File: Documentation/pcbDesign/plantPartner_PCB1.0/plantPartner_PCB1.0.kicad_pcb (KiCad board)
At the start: 2 copper layers, 271 x 152 mm, 76 parts, among them IC1 MPM3610, J1 Conn_01x04, J10 Screw_Terminal_01x03, J11 Conn_01x04, J12 Conn_01x03, J13 Conn_01x03, J14 Conn_01x03, J15 Conn_01x03, J16 Conn_01x04, J17 Conn_01x03, J18 Screw_Terminal_01x02, J19 Barrel_Jack, J2 Conn_01x04, J20 Conn_02x04_Top_Bottom, J21 Conn_01x04, J22 Conn_01x04, J23 Conn_01x02, J24 Conn_01x04, J25 Conn_01x04, J26 Conn_01x01, J27 Conn_01x03, J3 Conn_01x04, J4 Screw_Terminal, J5 Conn_01x02, J6 Screw_Terminal_01x03, J7 Conn_01x03, J8 Conn_02x04_Top_Bottom, J9 Conn_01x03, K1 SRD-05VDC-SL-C, K2 SRD-05VDC-SL-C, Q1 PNP, Q2 PNP, U1 EL357N-G, U2 MAX485, U3 ESP32-DEVKIT-V1, U4 EL357N-G

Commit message: Finished RS485 Transceiver, working on Buck Converter and connecting signals
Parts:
- removed J24: Conn_01x04, Connector_PinHeader_2.54mm:PinHeader_1x04_P2.54mm_Vertical
- J11: value Conn_01x04 -> Conn_01x02; footprint Connector_PinHeader_2.54mm:PinHeader_1x04_P2.54mm_Vertical -> Connector_PinHeader_2.54mm:PinHeader_1x02_P2.54mm_Vertical
- moved J26 118.7 mm to (222.2, 54.5)
- moved J11 61.8 mm to (81.7, 46.6), turned to 180 degrees
- moved R24 54.3 mm to (245.5, 25.1), turned to 0 degrees
- moved J17 50.4 mm to (242.7, 37.8)
- moved J5 49.3 mm to (243.0, 25.0)
- moved J20 45.3 mm to (177.3, 59.1), turned to 180 degrees
- moved D5 45.1 mm to (229.3, 60.5)
- moved D7 45.1 mm to (234.6, 57.7)
- moved J13 45.1 mm to (252.3, 72.6)
- moved K2 45.1 mm to (246.1, 62.7)
- moved Q2 45.1 mm to (234.3, 61.5)
- moved R18 45.1 mm to (229.0, 65.7)
- moved R20 45.1 mm to (235.3, 65.0)
- moved U4 45.1 mm to (231.8, 68.5)
- moved D6 45.1 mm to (234.7, 55.3)
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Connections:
- J11 pad 1: /B -> GND
- J11 pad 2: /A -> +12V
- J20 pad 3: /ADC1_5/Touch8 -> /ADC1_4/Touch9
- J20 pad 4: /ADC2_0/Touch0 -> /ADC1_5/Touch8
- J20 pad 8: /ADC1_4/Touch9 -> /ADC2_0/Touch0
- J26 pad 1: +12V -> /PWM_WATER_PIN
- J27 pad 1: +12V -> /PWM_FERTIL_PIN
- U1 pad 2: +12V -> /PWM_FERTIL_PIN
- U3 pad 27: +12V -> /PWM_WATER_PIN
- U3 pad 28: +12V -> /PWM_FERTIL_PIN
- U4 pad 2: +12V -> /PWM_WATER_PIN
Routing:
- net +12V: track 44.1 -> 101.1 mm, vias 0 -> 2
- net /ADC2_0/Touch0: track 0.00 -> 51.8 mm
- net /PWM_WATER_PIN: track 0.00 -> 19.5 mm
- net /B: track 2.79 -> 19.2 mm
- net /ADC1_6: track 0.00 -> 15.4 mm
- net /A: track 2.76 -> 17.6 mm
- net /ADC2_8/DAC1: track 0.00 -> 14.7 mm
- net /ADC2_7/Touch7: track 0.00 -> 14.6 mm
- net /ADC1_4/Touch9: track 0.00 -> 14.3 mm
- net GND: track 95.1 -> 107.2 mm
- net /ADC2_9/DAC2: track 0.00 -> 12.0 mm
- net /ADC1_7: track 0.00 -> 11.8 mm
- net /ADC1_5/Touch8: track 0.00 -> 11.0 mm
- net /H: track 8.19 -> 15.9 mm
- net +5V: track 28.1 -> 22.6 mm
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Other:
- board size 271 x 152 mm -> 271 x 130.8 mm
- board text added: "A"
- board text added: "B"
- board text added: "DE"
- board text added: "DI"
- board text added: "RE"
- board text added: "RO"
- board text added: "RS485 Transceiver"

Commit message: Fixed Buck Converter and routed it. Connected more majority of ESP signals and some of the debugging pins. Brought the size of PCB down to about 1/2 of the original. My goal is to finish by today and optimize size in the 2nd gen
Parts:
- added J24: Conn_01x03, Connector_PinHeader_2.54mm:PinHeader_1x03_P2.54mm_Vertical, F.Cu at (163.1, 59.1)
- added J25: Conn_01x03, Connector_PinHeader_2.54mm:PinHeader_1x03_P2.54mm_Vertical, F.Cu at (132.6, 92.2)
- added J28: Conn_01x01, Connector_PinHeader_2.54mm:PinHeader_1x01_P2.54mm_Vertical, F.Cu at (168.1, 58.9)
- IC1: footprint MyCustomFootprints:MPM3610 -> MPM3610:MPM3610
- J23: value Conn_01x02 -> Conn_01x01; footprint Connector_PinHeader_2.54mm:PinHeader_1x02_P2.54mm_Vertical -> Connector_PinHeader_2.54mm:PinHeader_1x01_P2.54mm_Vertical
- J27: value Conn_01x03 -> Conn_01x01; footprint Connector_PinHeader_2.54mm:PinHeader_1x03_P2.54mm_Vertical -> Connector_PinHeader_2.54mm:PinHeader_1x01_P2.54mm_Vertical
- moved J21 110.2 mm to (105.7, 83.1), turned to 90 degrees
- moved J8 94.9 mm to (145.1, 56.1), turned to -90 degrees
- moved J5 64.3 mm to (194.3, 67.0)
- moved R24 64.3 mm to (196.8, 67.1)
- moved J23 63.9 mm to (157.6, 93.8)
- moved J16 62.3 mm to (178.9, 96.8)
- moved J17 62.2 mm to (187.1, 65.8)
- moved D10 54.5 mm to (157.6, 91.2), turned to 180 degrees
- moved R22 54.1 mm to (157.6, 90.5), turned to 0 degrees
- moved J20 48.9 mm to (145.0, 95.8), turned to 90 degrees
- moved C1 46.7 mm to (174.9, 102.7)
- moved C2 46.7 mm to (169.9, 102.4)
- moved R1 46.7 mm to (172.0, 99.6)
- moved R2 46.7 mm to (169.8, 101.2)
- moved R3 46.7 mm to (169.7, 100.3)
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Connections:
- IC1 pad 11: /BST -> GND
- IC1 pad 18: /AAM -> GND
- IC1 pad 4: /SW -> GND
- IC1 pad 5: /SW -> GND
- IC1 pad 6: /SW -> GND
- J20 pad 8: /ADC2_0/Touch0 -> GND
- J23 pad 1: /ESP_EN -> /EXTERNAL LED
- J8 pad 3: /MISO/VSPI_MISO -> GND
- J8 pad 4: GND -> /MISO/VSPI_MISO
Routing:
- net GND: track 107.2 -> 180.0 mm
- net /RO: track 5.76 -> 77.6 mm, vias 0 -> 2
- net /DI: track 5.09 -> 61.6 mm, vias 0 -> 1
- net /DE: track 7.25 -> 55.4 mm, vias 0 -> 1
- net /ADC2_0/Touch0: track 51.8 -> 3.84 mm
- net +5V: track 22.6 -> 47.8 mm
- net +12V: track 101.1 -> 123.6 mm
- net /MOSI: track 0.00 -> 18.4 mm
- net /SCL: track 0.00 -> 12.3 mm
- net /PWM_FERTIL_PIN: track 0.00 -> 10.3 mm
- net /VSPI_CS: track 0.00 -> 8.95 mm
- net /EXTERNAL LED: track 0.00 -> 8.02 mm
- net /RX0: track 0.00 -> 7.90 mm
- net /ADC2_8/DAC1: track 14.7 -> 8.56 mm
- net /ADC2_7/Touch7: track 14.6 -> 8.66 mm
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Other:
- board size 271 x 130.8 mm -> 174.6 x 72.6 mm

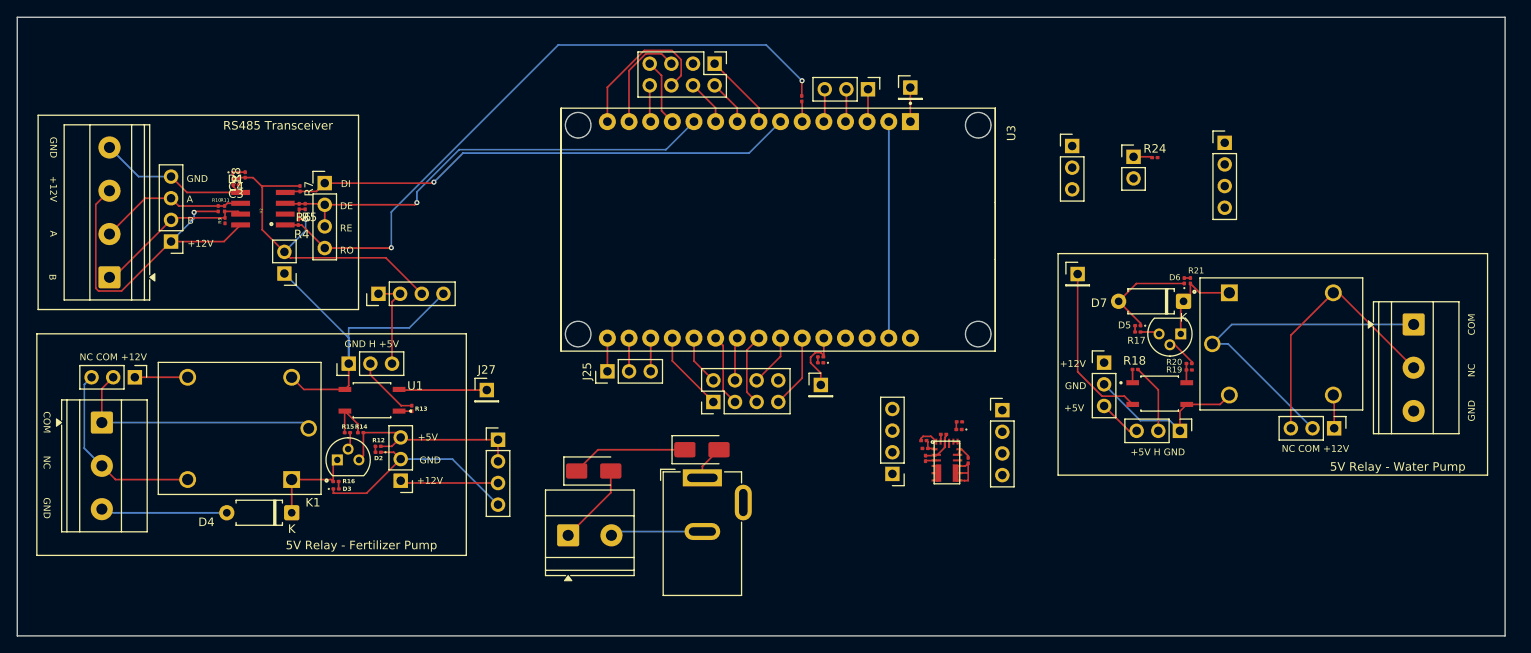
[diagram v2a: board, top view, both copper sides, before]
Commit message: Finished Routing (for now). I need to add silkscreens for debugging, then copper pour and probably other stuff. My goal is so have a JLCPCB order by tomorrow. I brought the PCB down to about the size of my phone
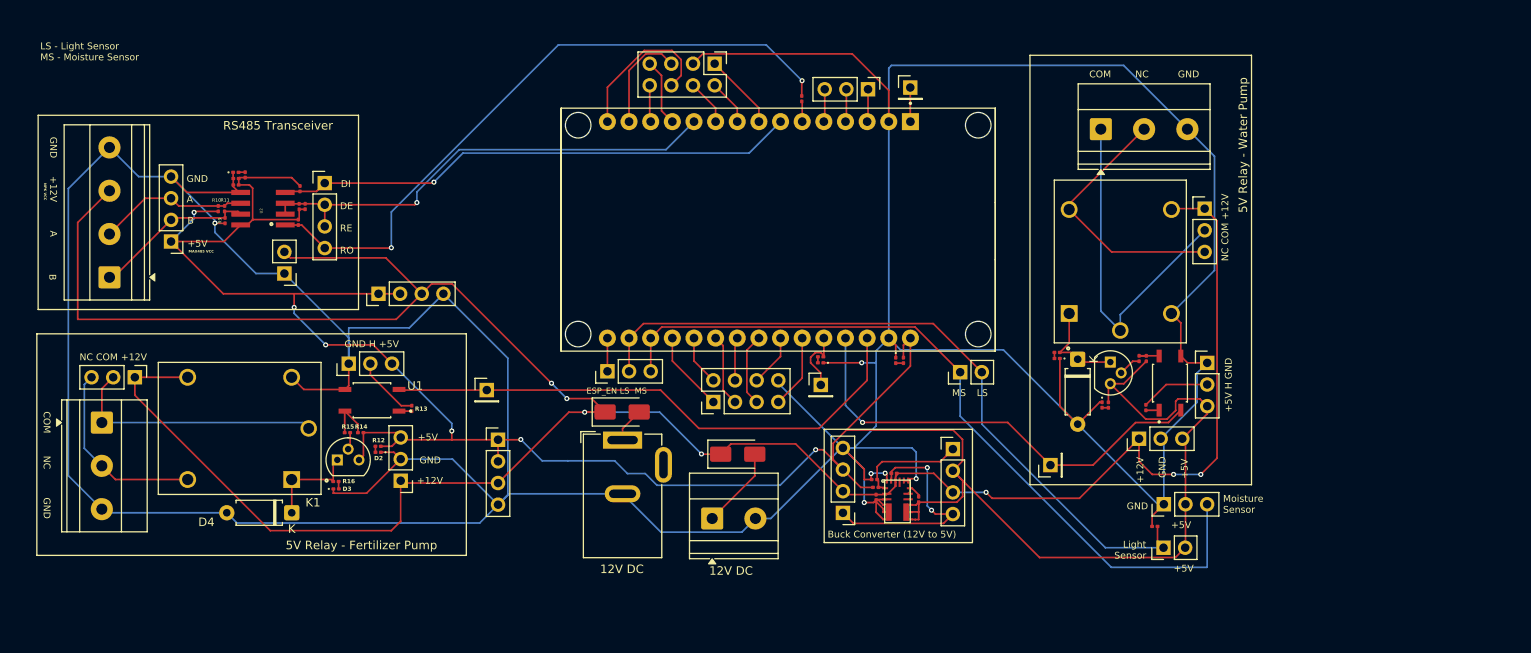
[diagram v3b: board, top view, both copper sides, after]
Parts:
- removed the J25 at (205.0, 65.4)
- added J29: Conn_01x02, Connector_PinHeader_2.54mm:PinHeader_1x02_P2.54mm_Vertical, F.Cu at (174.0, 92.3)
- moved J5 46.0 mm to (197.8, 112.9), turned to 90 degrees
- moved J17 43.4 mm to (197.9, 107.8), turned to 90 degrees
- moved J10 43.3 mm to (190.5, 63.8), turned to 0 degrees
- moved R24 43.3 mm to (196.8, 110.4), turned to 180 degrees
- moved J13 29.9 mm to (202.7, 73.1), turned to 0 degrees
- moved J26 22.7 mm to (184.6, 103.2), turned to 90 degrees
- moved K2 21.2 mm to (192.8, 79.3), turned to 90 degrees
- moved R21 17.8 mm to (185.3, 90.0), turned to 180 degrees
- moved D6 17.5 mm to (185.3, 90.7), turned to 180 degrees
- moved J18 17.0 mm to (144.9, 109.5)
- moved D9 17.0 mm to (147.9, 101.9)
- moved D7 14.2 mm to (187.8, 90.8), turned to -90 degrees
- moved D11 11.0 mm to (166.4, 90.9), turned to -90 degrees
- moved D8 10.4 mm to (134.3, 97.0)
- moved J19 10.4 mm to (134.3, 100.3)
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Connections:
- C3 pad 1: +12V -> +5V
- C4 pad 1: +12V -> +5V
- J3 pad 1: +12V -> +5V
- R10 pad 1: +12V -> +5V
- R4 pad 1: +12V -> +5V
- R5 pad 1: +12V -> +5V
- R6 pad 1: +12V -> +5V
- R7 pad 1: +12V -> +5V
- R8 pad 1: +12V -> +5V
- U2 pad 8: +12V -> +5V
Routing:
- net GND: track 180.0 -> 563.4 mm, vias 0 -> 6
- net +5V: track 47.8 -> 298.1 mm, vias 0 -> 6
- net +12V: track 123.6 -> 307.4 mm, vias 2 -> 7
- net /ADC_MOISTURE_SENSOR: track 3.90 -> 91.8 mm
- net /ADC_LIGHT_SENSOR: track 6.12 -> 84.6 mm
- net /PWM_FERTIL_PIN: track 10.3 -> 64.1 mm
- net /PWM_WATER_PIN: track 19.5 -> 52.8 mm, vias 0 -> 1
- net /EN: track 0.87 -> 27.2 mm, vias 0 -> 2
- net /FB: track 1.86 -> 13.1 mm
- net /DE: track 55.4 -> 56.6 mm
- net Net-(R19-Pad2): track 2.28 -> 3.26 mm
- net Net-(Q2-B): track 3.60 -> 2.68 mm
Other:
- board outline removed
- board text added: "12V DC"
- board text added: "Buck Converter (12V to 5V)"
- board text added: "ESP_EN LS MS"
- board text added: "LS"
- board text added: "LS - Light Sensor MS - Moisture Sensor"
- board text added: "Light Sensor"
- board text added: "MAX485 VCC"
- board text added: "MS"
- board text added: "Moisture Sensor"
- board text added: "NPK VCC"

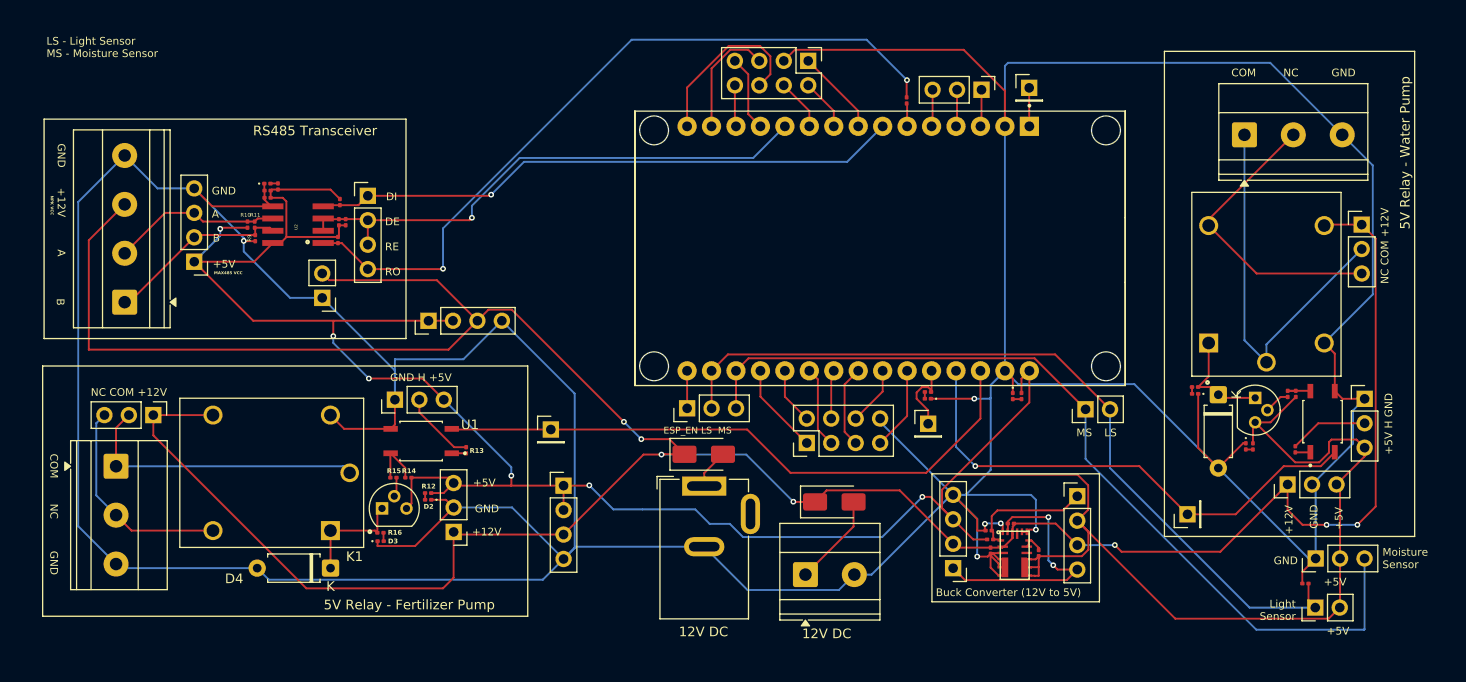
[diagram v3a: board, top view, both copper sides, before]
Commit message: Finished Labeling PCB (too much) and fixed DRC errors on PCB. Time to add copper pours, drill holes, and probably more, then review it with a TA, and make the order :)
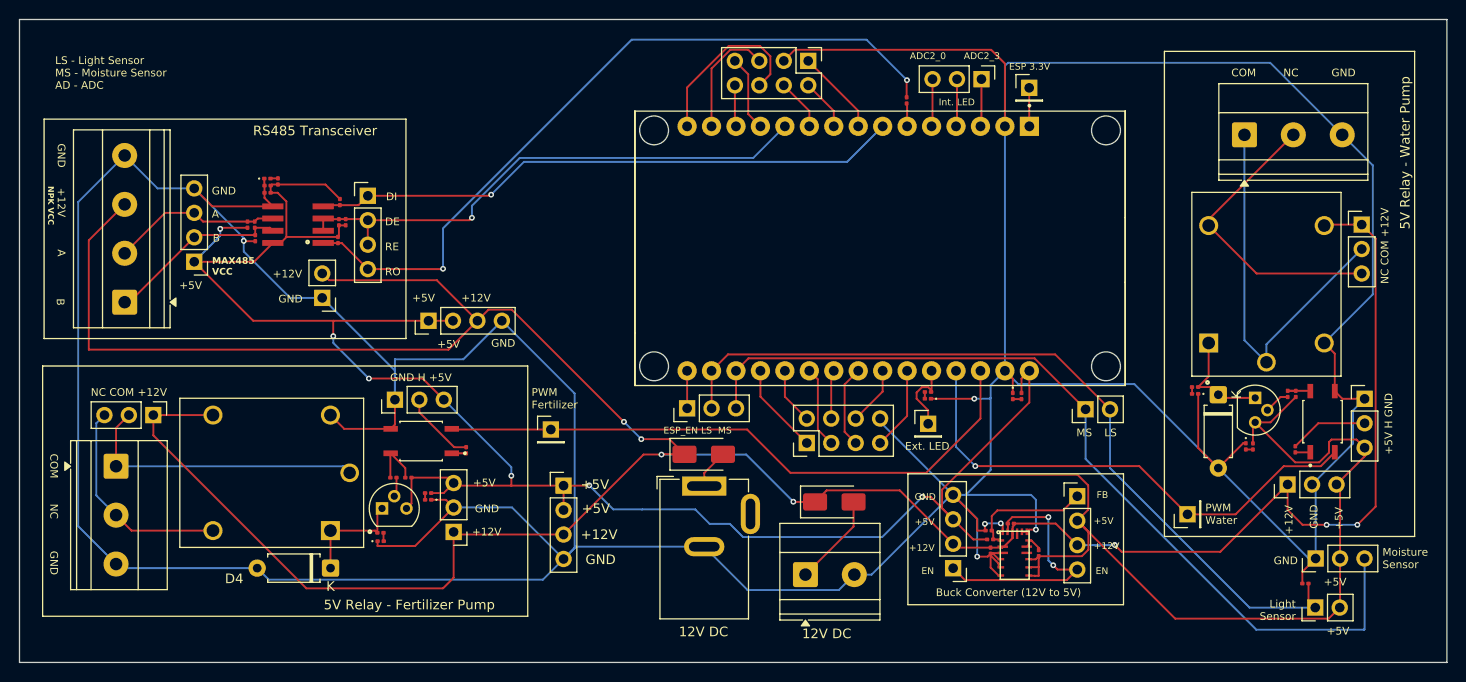
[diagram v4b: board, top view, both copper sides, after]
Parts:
- moved J24 1.10 mm to (163.1, 58.0)
- moved C3 0.52 mm to (89.0, 69.8)
- moved C4 0.52 mm to (89.0, 69.1)
- moved R8 0.52 mm to (90.1, 68.6)
- moved D1 0.52 mm to (89.0, 68.3)
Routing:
- net GND: track 563.4 -> 565.6 mm
- net /ADC2_3/Touch3: track 3.84 -> 5.09 mm
- net /INTERNAL LED: track 3.84 -> 5.09 mm
- net /ADC2_0/Touch0: track 3.84 -> 5.09 mm
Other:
- board outline added: 148.3 x 66.8 mm
- board text added: "AD2_7 AD2_8 AD1_4 AD1_6"
- board text added: "ADC2_0"
- board text added: "ADC2_3"
- board text added: "C1"
- board text added: "C2"
- board text added: "C3"
- board text added: "C4"
- board text added: "D1"
- board text added: "D10"
- board text added: "D11"
- board text added: "D4"
- board text added: "D5"
- board text added: "D6"
- board text added: "D7"
- board text added: "EN"
- board text added: "ESP 3.3V"
- board text added: "Ext. LED"
- board text added: "FB"
- board text added: "Fertilizer"
- board text added: "GND AD2_9 AD1_5 AD1_7"
- board text added: "Int. LED"
- board text added: "K2"
- board text added: "LS - Light Sensor MS - Moisture Sensor AD - ADC"
- board text added: "PWM"
- board text added: "Q1"
- board text added: "Q2"
- board text added: "R1"
- board text added: "R17"
- board text added: "R18"
- board text added: "R19"
- board text added: "R2"
- board text added: "R20"
- board text added: "R21"
- board text added: "R22"
- board text added: "R23"
- board text added: "R24"
- board text added: "R26"
- board text added: "R3"
- board text added: "R4"
- board text added: "R5"
- board text added: "R6"
- board text added: "R7"
- board text added: "R8"
- board text added: "SCK MISO MOSI TX0"
- board text added: "U4"
- board text added: "VSPI_CS GND SCL RXO"
- board text added: "Water"
- board text removed: "LS - Light Sensor MS - Moisture Sensor"
